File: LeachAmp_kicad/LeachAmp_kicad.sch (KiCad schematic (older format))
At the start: 118 parts, among them J1 Conn_01x04_Male, J2 Conn_01x02_Male, J3 Conn_01x03_Female, Q1 BC546, Q10 MPSA06, Q11 MPSA56, Q12 BF470, Q13 BF469, Q14 2N3439, Q15 2N5416, Q16 MJE15030, Q17 MJE15031, Q18 NJL3281D, Q19 NJL1302D, Q2 BC546, Q20 NJL3281D, Q21 NJL1302D, Q3 BC556, Q4 BC556, Q5 BC546, Q6 BC556, Q7 MPSA06, Q8 BC556, Q9 BC546

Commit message: Schéma komplet + DPS v progresu
Kompletní schéma Leach verze.
DPS rozpracované - silová část
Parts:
- removed J1: Conn_01x04_Male, Connector_Wago:Wago_734-164_1x04_P3.50mm_Horizontal, symbol Connector:Conn_01x04_Male
- removed J2: Conn_01x02_Male, Connector_Wago:Wago_734-162_1x02_P3.50mm_Horizontal, symbol Connector:Conn_01x02_Male
- removed unit 1 of Q18
- removed unit 1 of Q19
- removed unit 1 of Q20
- removed unit 1 of Q21
- removed R26: 1k, Resistor_THT:R_Axial_DIN0207_L6.3mm_D2.5mm_P10.16mm_Horizontal, symbol Device:R
- added J1: Conn_01x12_Female, LeachAmp_library:Wago-256-406, symbol Connector:Conn_01x12_Female
- added J2: Conn_01x04_Female, LeachAmp_library:Wago-256-402, symbol Connector:Conn_01x04_Female
- added T1, T3: MJL3281, Package_TO_SOT_THT:TO-264-3_Horizontal_TabDown, symbol Transistor_BJT:2N3055
- added T2, T4: MJL3201, Package_TO_SOT_THT:TO-264-3_Horizontal_TabDown, symbol Transistor_BJT:MPSA92
- F1, F2: footprint Fuse:Fuseholder_Cylinder-5x20mm_Schurter_0031_8201_Horizontal_Open -> Fuse_Holders_and_Fuses:Fuseholder5x20_horiz_SemiClosed_Casing10x25mm
- Q14: value 2N3439 -> BF469; footprint Package_TO_SOT_THT:TO-92_Inline -> Package_TO_SOT_THT:TO-126-3_Horizontal_TabDown
- Q15: value 2N5416 -> BF470; footprint Package_TO_SOT_THT:TO-92_Inline -> Package_TO_SOT_THT:TO-126-3_Horizontal_TabDown
- Q7: value MPSA06 -> BD139
- R1: value 20k -> 22k
- R2: value 2k -> 2k2
- R25: value 1k -> 8k2
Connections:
- wire segments 351 -> 376
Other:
- moved on the sheet: R25, R27, RV1

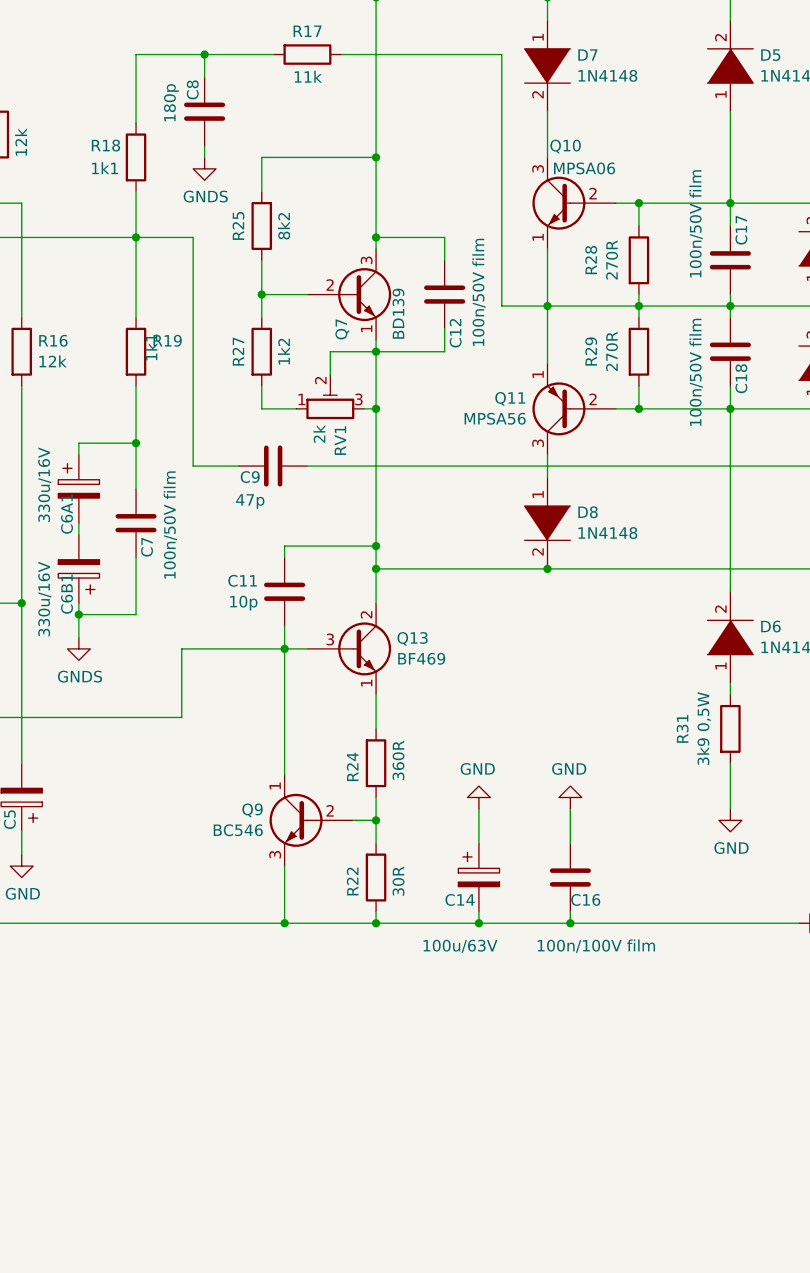
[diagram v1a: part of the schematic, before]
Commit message: DPS progress 70%
DPS z většiny zpracovaná:
Výkonová část 85 %;
signální 60 %;
zpětná vazba 20 %.
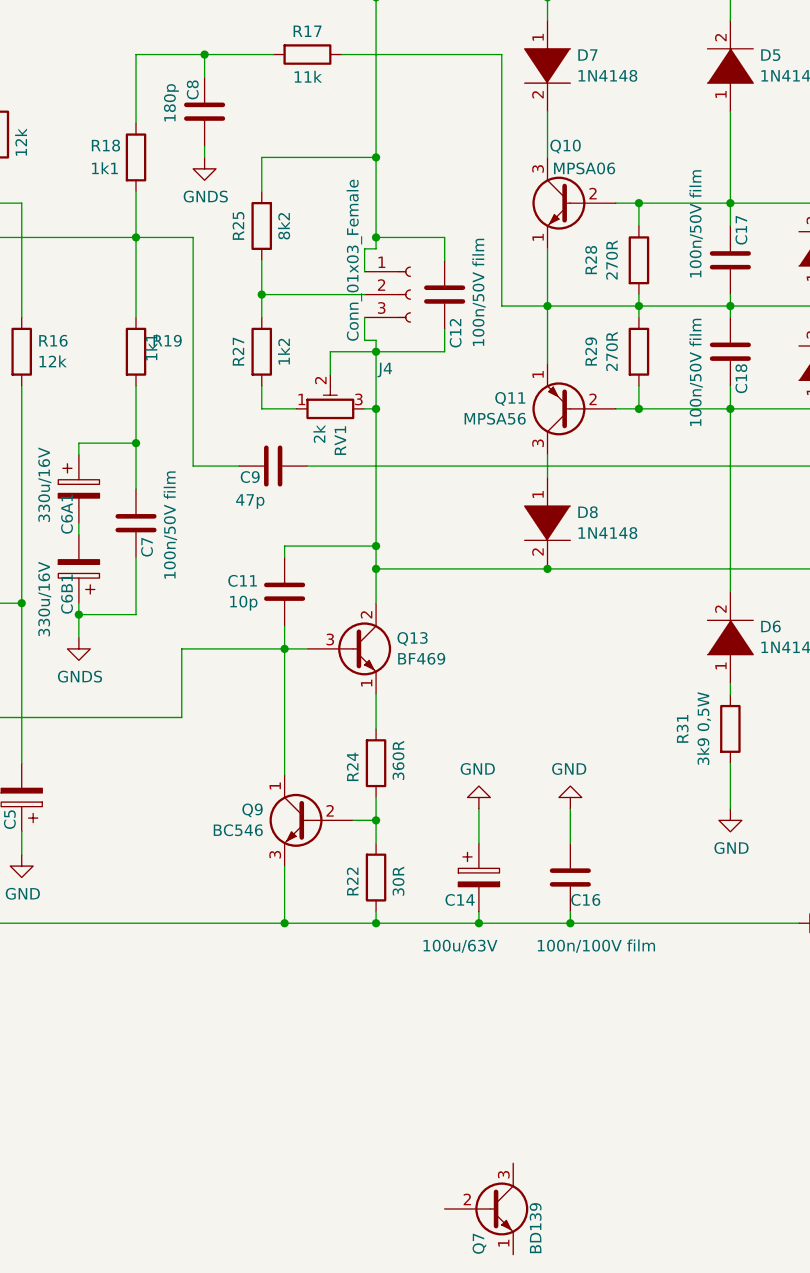
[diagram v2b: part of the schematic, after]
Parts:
- added J4: Conn_01x03_Female, Connector_Molex:Molex_KK-254_AE-6410-03A_1x03_P2.54mm_Vertical, symbol Connector:Conn_01x03_Female
- Q12, Q13: footprint Package_TO_SOT_THT:TO-126-3_Horizontal_TabDown -> Package_TO_SOT_THT:TO-126-3_Vertical
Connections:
- wire segments 376 -> 380
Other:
- moved on the sheet: Q7
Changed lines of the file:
@@
 L Transistor_BJT:MPSA42 Q7
 U 1 1 5FE9C58A
-P 5850 4400
-F 0 "Q7" V 5800 4200 50  0000 L CNN
-F 1 "BD139" V 6050 4200 50  0000 L CNN
-F 2 "Package_TO_SOT_THT:TO-92_Inline" H 6050 4325 50  0001 L CIN
-F 3 "http://www.onsemi.com/pub_link/Collateral/MPSA42-D.PDF" H 5850 4400 50  0001 L CNN
-	1    5850 4400
+P 6450 8400
+F 0 "Q7" V 6400 8200 50  0000 L CNN
+F 1 "BD139" V 6650 8200 50  0000 L CNN
+F 2 "Package_TO_SOT_THT:TO-92_Inline" H 6650 8325 50  0001 L CIN
+F 3 "http://www.onsemi.com/pub_link/Collateral/MPSA42-D.PDF" H 6450 8400 50  0001 L CNN
+	1    6450 8400
 	1    0    0    -1
 $EndComp
@@
 Wire Wire Line
 	5450 4500 5450 4400
-Wire Wire Line
-	5650 4400 5450 4400
 $Comp
 L Device:R R27
@@
 F 0 "Q13" H 6040 5996 50  0000 L CNN
 F 1 "BF469" H 6040 5905 50  0000 L CNN
-F 2 "Package_TO_SOT_THT:TO-126-3_Horizontal_TabDown" H 6050 5875 50  0001 L CIN
+F 2 "Package_TO_SOT_THT:TO-126-3_Vertical" H 6050 5875 50  0001 L CIN
 F 3 "https://www.pcpaudio.com/pcpfiles/transistores/BF457-8-9.pdf" H 5850 5950 50  0001 L CNN
 	1    5850 5950
@@
 F 0 "Q12" H 6040 2604 50  0000 L CNN
 F 1 "BF470" H 6040 2695 50  0000 L CNN
-F 2 "Package_TO_SOT_THT:TO-126-3_Horizontal_TabDown" H 6050 2575 50  0001 L CIN
+F 2 "Package_TO_SOT_THT:TO-126-3_Vertical" H 6050 2575 50  0001 L CIN
 F 3 "http://pdf.datasheetcatalog.com/datasheet/sanyo/ds_pdf_e/2SB631.pdf" H 5850 2650 50  0001 L CNN
 	1    5850 2650
@@
 Wire Wire Line
 	14500 4650 14500 4550
+$Comp
+L Connector:Conn_01x03_Female J4
+U 1 1 5FFA5831
+P 6100 4400
+F 0 "J4" H 5992 4075 50  0000 C CNN
+F 1 "Conn_01x03_Female" V 5850 4550 50  0000 C CNN
+F 2 "Connector_Molex:Molex_KK-254_AE-6410-03A_1x03_P2.54mm_Vertical" H 6100 4400 50  0001 C CNN
+F 3 "~" H 6100 4400 50  0001 C CNN
+	1    6100 4400
+	1    0    0    -1
+$EndComp
+Wire Wire Line
+	5450 4400 5900 4400
+Wire Wire Line
+	5950 4600 5900 4600
+Wire Wire Line
+	5900 4600 5900 4500
+Wire Wire Line
+	5900 4300 5900 4200
+Wire Wire Line
+	5900 4200 5950 4200
 $EndSCHEMATC

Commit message: DPS progress 90 %
DPS z většiny zpracovaná:
Výkonová část 85 %;
signální 80 %;
zpětná vazba 40 %.
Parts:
- removed Q18, Q20: NJL3281D, Package_TO_SOT_THT:TO-264-5_Horizontal_TabDown, symbol Leach_lib:NJL3281D
- removed Q19, Q21: NJL1302D, Package_TO_SOT_THT:TO-264-5_Horizontal_TabDown, symbol Leach_lib:NJL1302D
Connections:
- net labels removed: A, B
- wire segments 380 -> 375
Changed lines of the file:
@@
-	0    -1   -1   0
-$EndComp
-$Comp
-L Leach_lib:NJL3281D Q18
-U 2 1 601DC0BD
-P 8550 1000
-F 0 "Q18" V 8765 1000 50  0000 C CNN
-F 1 "NJL3281D" V 8674 1000 50  0000 C CNN
-F 2 "Package_TO_SOT_THT:TO-264-5_Horizontal_TabDown" H 8800 0   50  0001 C CNN
-F 3 "" H 8400 1200 50  0001 C CNN
-	2    8550 1000
-	0    -1   -1   0
-$EndComp
-$Comp
-L Leach_lib:NJL3281D Q20
-U 2 1 6021024D
-P 9050 1000
-F 0 "Q20" V 9265 1000 50  0000 C CNN
-F 1 "NJL3281D" V 9174 1000 50  0000 C CNN
-F 2 "Package_TO_SOT_THT:TO-264-5_Horizontal_TabDown" H 9300 0   50  0001 C CNN
-F 3 "" H 8900 1200 50  0001 C CNN
-	2    9050 1000
-	0    -1   -1   0
-$EndComp
-Text GLabel 8150 1000 0    50   Input ~ 0
-A
-Text GLabel 10400 1000 2    50   Input ~ 0
-B
-Wire Wire Line
-	8150 1000 8400 1000
-Wire Wire Line
-	8700 1000 8900 1000
-Wire Wire Line
-	10100 1000 10400 1000
-$Comp
-L Leach_lib:NJL1302D Q19
-U 2 1 6030D30F
-P 9500 1000
-F 0 "Q19" V 9715 1000 50  0000 C CNN
-F 1 "NJL1302D" V 9624 1000 50  0000 C CNN
-F 2 "Package_TO_SOT_THT:TO-264-5_Horizontal_TabDown" H 9350 1400 50  0001 C CNN
-F 3 "" H 9350 1400 50  0001 C CNN
-	2    9500 1000
-	0    -1   -1   0
-$EndComp
-$Comp
-L Leach_lib:NJL1302D Q21
-U 2 1 6030E656
-P 9950 1000
-F 0 "Q21" V 10165 1000 50  0000 C CNN
-F 1 "NJL1302D" V 10074 1000 50  0000 C CNN
-F 2 "Package_TO_SOT_THT:TO-264-5_Horizontal_TabDown" H 9800 1400 50  0001 C CNN
-F 3 "" H 9800 1400 50  0001 C CNN
-	2    9950 1000
 	0    -1   -1   0
 $EndComp
 Wire Wire Line
-	9650 1000 9800 1000
-Wire Wire Line
-	9200 1000 9350 1000
-Wire Wire Line
 	10400 1450 10850 1450

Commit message: Dokumentace
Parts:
- added J?: Conn_01x03_Female, Connector_Molex:Molex_KK-254_AE-6410-03A_1x03_P2.54mm_Vertical, symbol Connector:Conn_01x03_Female
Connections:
- net at Q7.1 (E): now also J?.1 (Pin_1)
- net at Q7.2 (B): now also J?.2 (Pin_2)
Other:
- moved on the sheet: C1, C10, C11, C12, C13, C14, C15, C16, C17, C18, C19, C2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
